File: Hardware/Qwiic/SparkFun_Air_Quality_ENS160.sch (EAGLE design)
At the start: 32 parts, among them J1 QWIIC_RIGHT_ANGLE, J2 QWIIC_RIGHT_ANGLE, U1 AP2127K-1.8V, U24 ENS-160

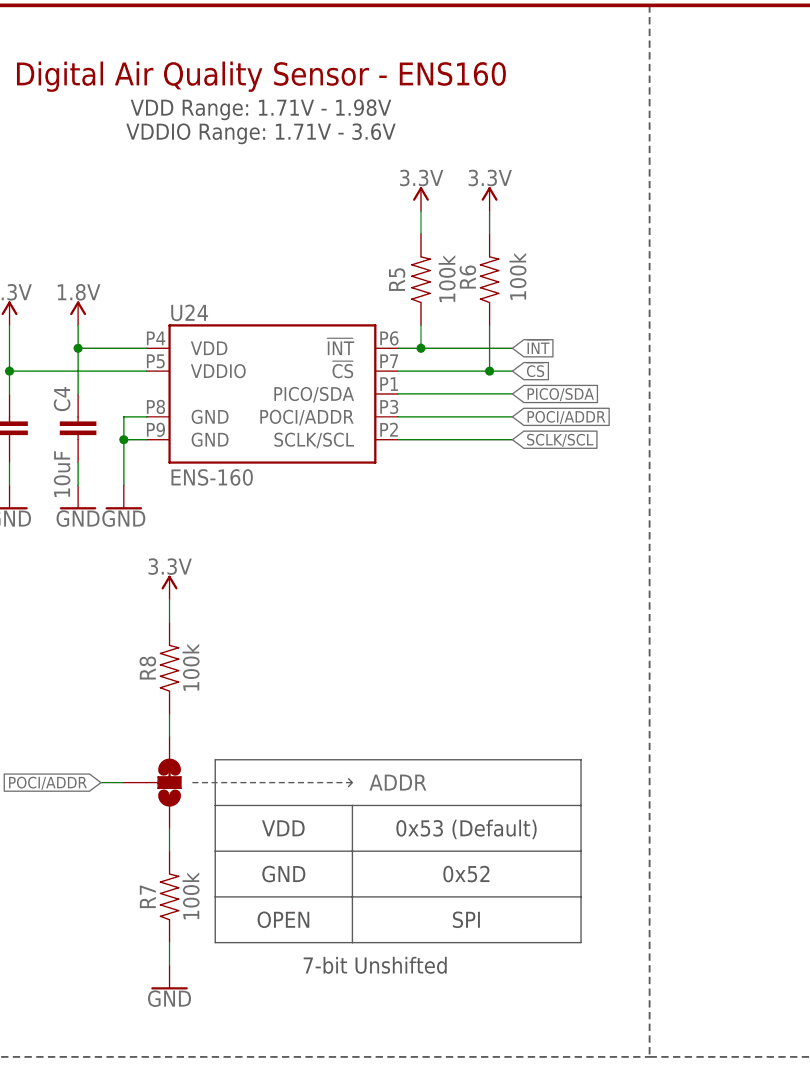
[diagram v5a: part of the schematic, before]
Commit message: Changes all values to 10k, removes pull up on interrupt
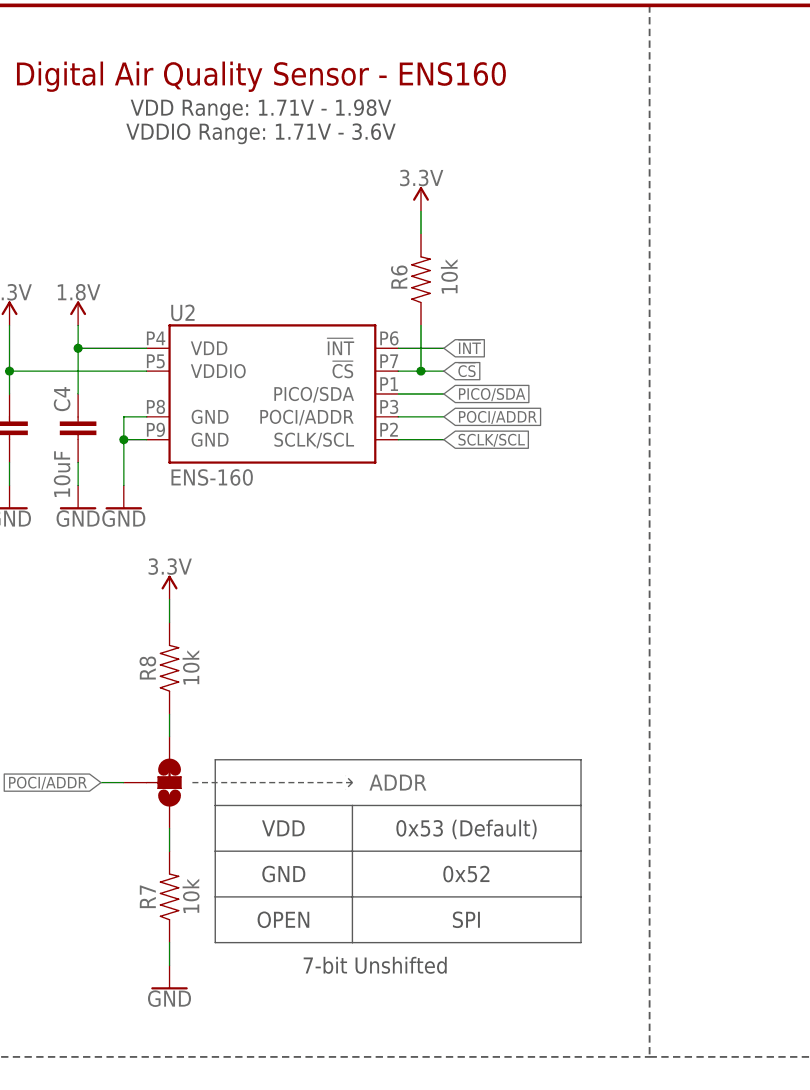
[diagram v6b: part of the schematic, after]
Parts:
- removed R5: 100k, SparkFun-Resistors:100KOHM-0603-1/10W-1%
- R6, R7, R8: value 100k -> 10k; device SparkFun-Resistors:100KOHM-0603-1/10W-1% -> SparkFun-Resistors:10KOHM-0603-1/10W-1%
- renumbered U24 to U2
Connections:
- net !INT!: no longer R5.1
- net 3.3V: no longer R5.2
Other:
- moved on the sheet: R6
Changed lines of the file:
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@@
 <part name="FD4" library="SparkFun-Aesthetics" deviceset="FIDUCIAL" device="1X2"/>
 <part name="LOGO4" library="SparkFun-Aesthetics" deviceset="QWIIC_LOGO" device="_4MM"/>
-<part name="U24" library="ENS160" deviceset="ENS-160" device=""/>
+<part name="U2" library="ENS160" deviceset="ENS-160" device=""/>
 <part name="U1" library="SparkFun-IC-Power" deviceset="V_REG_AP2127" device="K-1.8V" value="AP2127K-1.8V"/>
 <part name="C1" library="SparkFun-Capacitors" deviceset="1.0UF" device="-0603-16V-10%" value="1.0uF"/>
@@
 <part name="SUPPLY8" library="SparkFun-PowerSymbols" deviceset="3.3V" device=""/>
 <part name="GND5" library="SparkFun-PowerSymbols" deviceset="GND" device=""/>
-<part name="R5" library="SparkFun-Resistors" deviceset="100KOHM" device="-0603-1/10W-1%" value="100k"/>
-<part name="R6" library="SparkFun-Resistors" deviceset="100KOHM" device="-0603-1/10W-1%" value="100k"/>
-<part name="SUPPLY9" library="SparkFun-PowerSymbols" deviceset="3.3V" device=""/>
+<part name="R6" library="SparkFun-Resistors" deviceset="10KOHM" device="-0603-1/10W-1%" value="10k"/>
 <part name="SUPPLY10" library="SparkFun-PowerSymbols" deviceset="3.3V" device=""/>
 <part name="J3" library="SparkFun-Connectors" deviceset="CONN_07" device="NO_SILK"/>
@@
 <part name="GND8" library="SparkFun-PowerSymbols" deviceset="GND" device=""/>
 <part name="ADDR" library="SparkFun-Jumpers" deviceset="JUMPER-SMT_3_1-NC_TRACE" device="_SILK" package3d_urn="urn:adsk.eagle:package:39288/1"/>
-<part name="R7" library="SparkFun-Resistors" deviceset="100KOHM" device="-0603-1/10W-1%" value="100k"/>
-<part name="R8" library="SparkFun-Resistors" deviceset="100KOHM" device="-0603-1/10W-1%" value="100k"/>
+<part name="R7" library="SparkFun-Resistors" deviceset="10KOHM" device="-0603-1/10W-1%" value="10k"/>
+<part name="R8" library="SparkFun-Resistors" deviceset="10KOHM" device="-0603-1/10W-1%" value="10k"/>
 <part name="SUPPLY11" library="SparkFun-PowerSymbols" deviceset="3.3V" device=""/>
 <part name="GND9" library="SparkFun-PowerSymbols" deviceset="GND" device=""/>
@@
 <instance part="FD4" gate="G$1" x="243.84" y="27.94" smashed="yes"/>
 <instance part="LOGO4" gate="G$1" x="180.34" y="40.64" smashed="yes"/>
-<instance part="U24" gate="G$1" x="43.18" y="142.24" smashed="yes">
+<instance part="U2" gate="G$1" x="43.18" y="142.24" smashed="yes">
 <attribute name="NAME" x="33.02" y="150.368" size="1.778" layer="95" font="vector"/>
 <attribute name="VALUE" x="33.02" y="132.08" size="1.778" layer="96" font="vector"/>
@@
 <attribute name="VALUE" x="27.94" y="129.286" size="1.778" layer="96" font="vector" align="top-center"/>
 </instance>
-<instance part="R5" gate="G$1" x="60.96" y="154.94" smashed="yes" rot="R90">
-<attribute name="NAME" x="59.182" y="154.94" size="1.778" layer="95" font="vector" rot="R90" align="bottom-center"/>
-<attribute name="VALUE" x="62.992" y="154.94" size="1.778" layer="96" font="vector" rot="R90" align="top-center"/>
-</instance>
-<instance part="R6" gate="G$1" x="68.58" y="154.94" smashed="yes" rot="R90">
-<attribute name="NAME" x="67.056" y="155.194" size="1.778" layer="95" font="vector" rot="R90" align="bottom-center"/>
-<attribute name="VALUE" x="70.866" y="155.194" size="1.778" layer="96" font="vector" rot="R90" align="top-center"/>
-</instance>
-<instance part="SUPPLY9" gate="G$1" x="60.96" y="162.56" smashed="yes">
+<instance part="R6" gate="G$1" x="60.96" y="154.94" smashed="yes" rot="R90">
+<attribute name="NAME" x="59.436" y="155.194" size="1.778" layer="95" font="vector" rot="R90" align="bottom-center"/>
+<attribute name="VALUE" x="63.246" y="155.194" size="1.778" layer="96" font="vector" rot="R90" align="top-center"/>
+</instance>
+<instance part="SUPPLY10" gate="G$1" x="60.96" y="162.56" smashed="yes">
 <attribute name="VALUE" x="60.96" y="165.354" size="1.778" layer="96" font="vector" align="bottom-center"/>
-</instance>
-<instance part="SUPPLY10" gate="G$1" x="68.58" y="162.56" smashed="yes">
-<attribute name="VALUE" x="68.58" y="165.354" size="1.778" layer="96" font="vector" align="bottom-center"/>
 </instance>
 <instance part="J3" gate="J1" x="17.78" y="20.32" smashed="yes">
@@
 </segment>
 <segment>
-<pinref part="U24" gate="G$1" pin="GND@8"/>
+<pinref part="U2" gate="G$1" pin="GND@8"/>
 <wire x1="30.48" y1="139.7" x2="27.94" y2="139.7" width="0.1524" layer="91"/>
 <wire x1="27.94" y1="139.7" x2="27.94" y2="137.16" width="0.1524" layer="91"/>
-<pinref part="U24" gate="G$1" pin="GND@9"/>
+<pinref part="U2" gate="G$1" pin="GND@9"/>
 <wire x1="27.94" y1="137.16" x2="27.94" y2="132.08" width="0.1524" layer="91"/>
 <wire x1="30.48" y1="137.16" x2="27.94" y2="137.16" width="0.1524" layer="91"/>
@@
 <segment>
 <wire x1="15.24" y1="149.86" x2="15.24" y2="144.78" width="0.1524" layer="91"/>
-<pinref part="U24" gate="G$1" pin="VDDIO"/>
+<pinref part="U2" gate="G$1" pin="VDDIO"/>
 <wire x1="15.24" y1="144.78" x2="30.48" y2="144.78" width="0.1524" layer="91"/>
 <pinref part="SUPPLY8" gate="G$1" pin="3.3V"/>
@@
 </segment>
 <segment>
-<pinref part="R5" gate="G$1" pin="2"/>
+<pinref part="R6" gate="G$1" pin="2"/>
 <wire x1="60.96" y1="162.56" x2="60.96" y2="160.02" width="0.1524" layer="91"/>
-<pinref part="SUPPLY9" gate="G$1" pin="3.3V"/>
-</segment>
-<segment>
-<pinref part="R6" gate="G$1" pin="2"/>
-<wire x1="68.58" y1="162.56" x2="68.58" y2="160.02" width="0.1524" layer="91"/>
 <pinref part="SUPPLY10" gate="G$1" pin="3.3V"/>
 </segment>
@@
 <net name="!INT!" class="0">
 <segment>
-<pinref part="U24" gate="G$1" pin="!INT!"/>
-<wire x1="60.96" y1="147.32" x2="58.42" y2="147.32" width="0.1524" layer="91"/>
-<pinref part="R5" gate="G$1" pin="1"/>
-<wire x1="60.96" y1="149.86" x2="60.96" y2="147.32" width="0.1524" layer="91"/>
-<wire x1="71.12" y1="147.32" x2="60.96" y2="147.32" width="0.1524" layer="91"/>
-<junction x="60.96" y="147.32"/>
-<label x="71.12" y="147.32" size="1.27" layer="95" font="vector" xref="yes"/>
+<pinref part="U2" gate="G$1" pin="!INT!"/>
+<wire x1="63.5" y1="147.32" x2="58.42" y2="147.32" width="0.1524" layer="91"/>
+<label x="63.5" y="147.32" size="1.27" layer="95" font="vector" xref="yes"/>
 </segment>
 <segment>
@@
 </segment>
 <segment>
-<pinref part="U24" gate="G$1" pin="VDD"/>
+<pinref part="U2" gate="G$1" pin="VDD"/>
 <wire x1="22.86" y1="149.86" x2="22.86" y2="147.32" width="0.1524" layer="91"/>
 <wire x1="22.86" y1="147.32" x2="30.48" y2="147.32" width="0.1524" layer="91"/>
@@
 <net name="POCI/ADDR" class="0">
 <segment>
-<pinref part="U24" gate="G$1" pin="POCI/ADDR"/>
-<wire x1="71.12" y1="139.7" x2="58.42" y2="139.7" width="0.1524" layer="91"/>
-<label x="71.12" y="139.7" size="1.27" layer="95" font="vector" xref="yes"/>
+<pinref part="U2" gate="G$1" pin="POCI/ADDR"/>
+<wire x1="63.5" y1="139.7" x2="58.42" y2="139.7" width="0.1524" layer="91"/>
+<label x="63.5" y="139.7" size="1.27" layer="95" font="vector" xref="yes"/>
 </segment>
 <segment>
@@
 <net name="SCLK/SCL" class="0">
 <segment>
-<pinref part="U24" gate="G$1" pin="SCLK/SCL"/>
-<wire x1="71.12" y1="137.16" x2="58.42" y2="137.16" width="0.1524" layer="91"/>
-<label x="71.12" y="137.16" size="1.27" layer="95" font="vector" xref="yes"/>
+<pinref part="U2" gate="G$1" pin="SCLK/SCL"/>
+<wire x1="63.5" y1="137.16" x2="58.42" y2="137.16" width="0.1524" layer="91"/>
+<label x="63.5" y="137.16" size="1.27" layer="95" font="vector" xref="yes"/>
 </segment>
 <segment>
@@
 <net name="PICO/SDA" class="0">
 <segment>
-<pinref part="U24" gate="G$1" pin="PICO/SDA"/>
-<wire x1="71.12" y1="142.24" x2="58.42" y2="142.24" width="0.1524" layer="91"/>
-<label x="71.12" y="142.24" size="1.27" layer="95" font="vector" xref="yes"/>
+<pinref part="U2" gate="G$1" pin="PICO/SDA"/>
+<wire x1="63.5" y1="142.24" x2="58.42" y2="142.24" width="0.1524" layer="91"/>
+<label x="63.5" y="142.24" size="1.27" layer="95" font="vector" xref="yes"/>
 </segment>
 <segment>
@@
 <net name="!CS!" class="0">
 <segment>
-<pinref part="U24" gate="G$1" pin="!CS!"/>
-<wire x1="71.12" y1="144.78" x2="68.58" y2="144.78" width="0.1524" layer="91"/>
+<pinref part="U2" gate="G$1" pin="!CS!"/>
+<wire x1="63.5" y1="144.78" x2="60.96" y2="144.78" width="0.1524" layer="91"/>
 <pinref part="R6" gate="G$1" pin="1"/>
-<wire x1="68.58" y1="144.78" x2="58.42" y2="144.78" width="0.1524" layer="91"/>
-<wire x1="68.58" y1="149.86" x2="68.58" y2="144.78" width="0.1524" layer="91"/>
-<junction x="68.58" y="144.78"/>
-<label x="71.12" y="144.78" size="1.27" layer="95" font="vector" xref="yes"/>
-</segment>
-<segment>
+<wire x1="60.96" y1="144.78" x2="58.42" y2="144.78" width="0.1524" layer="91"/>
+<wire x1="60.96" y1="149.86" x2="60.96" y2="144.78" width="0.1524" layer="91"/>
+<junction x="60.96" y="144.78"/>
+<label x="63.5" y="144.78" size="1.27" layer="95" font="vector" xref="yes"/>
+</segment>
+<segment>

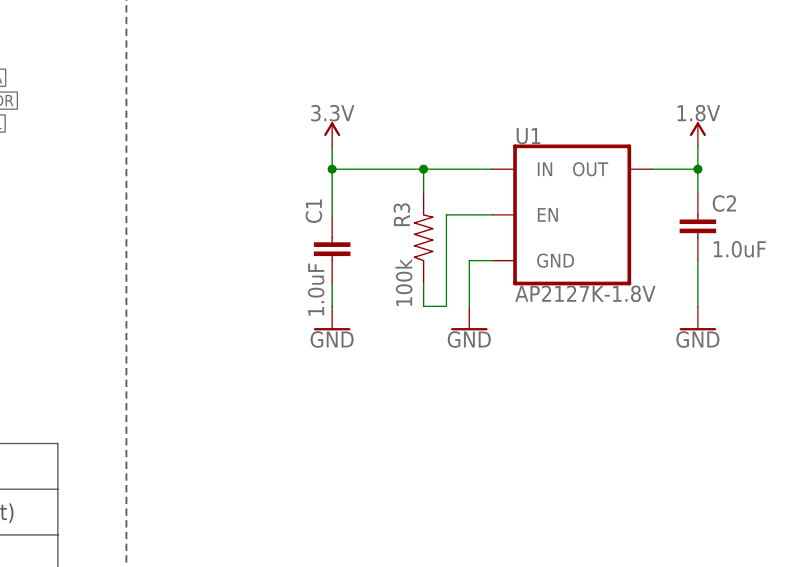
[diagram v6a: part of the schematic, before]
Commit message: Changes enable pin pullup to 10k on the VREG
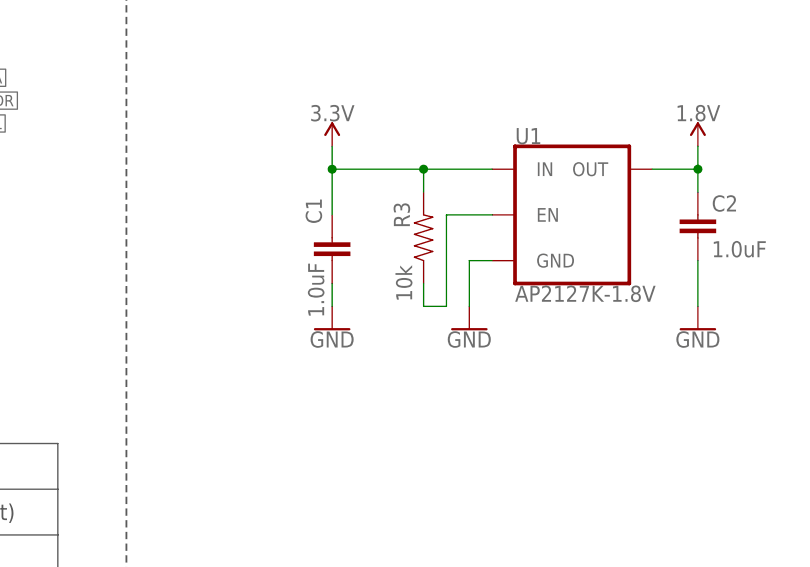
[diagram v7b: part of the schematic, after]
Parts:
- R3: value 100k -> 10k; device SparkFun-Resistors:100KOHM-0603-1/10W-1% -> SparkFun-Resistors:10KOHM-0603-1/10W-1%
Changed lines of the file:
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@@
 <part name="GND2" library="SparkFun-PowerSymbols" deviceset="GND" device=""/>
 <part name="GND4" library="SparkFun-PowerSymbols" deviceset="GND" device=""/>
-<part name="R3" library="SparkFun-Resistors" deviceset="100KOHM" device="-0603-1/10W-1%" value="100k"/>
+<part name="R3" library="SparkFun-Resistors" deviceset="10KOHM" device="-0603-1/10W-1%" value="10k"/>
 <part name="SUPPLY7" library="SparkFun-PowerSymbols" deviceset="1.8V" device=""/>
 <part name="SUPPLY8" library="SparkFun-PowerSymbols" deviceset="3.3V" device=""/>
